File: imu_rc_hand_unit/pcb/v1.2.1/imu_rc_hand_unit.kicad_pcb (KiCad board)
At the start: 2 copper layers, 35 x 50 mm, 76 parts, among them J1 USB_C_Receptacle_USB2.0_16P, J2 JST SH1.0, Q1 IRLML6344TRPBF, Q2 IRLML6344TRPBF, Q3 DMP3160L-7, Q4 IRLML6344TRPBF, Q5 DMP3160L-7, Q6 BSS138, Q7 BC817-25, Q8 BC817-25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

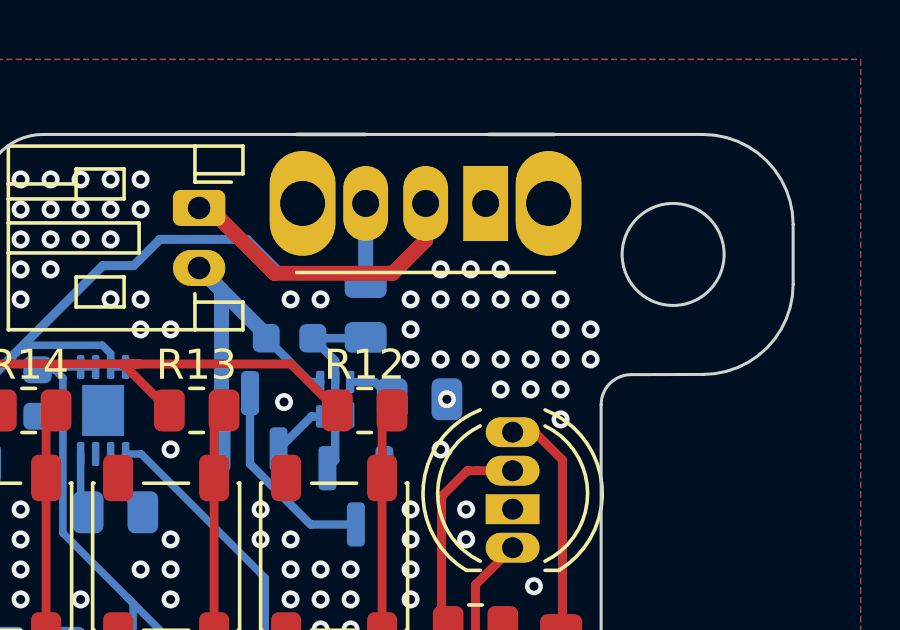
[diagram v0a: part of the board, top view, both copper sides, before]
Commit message: commit #39
imu rc hand unit v1.2.2:
removed bq297
added ON/OFF text for switch

enclosure hand unit:
small hole changes inside (m3) and outside (m3)
led diameter hole increased
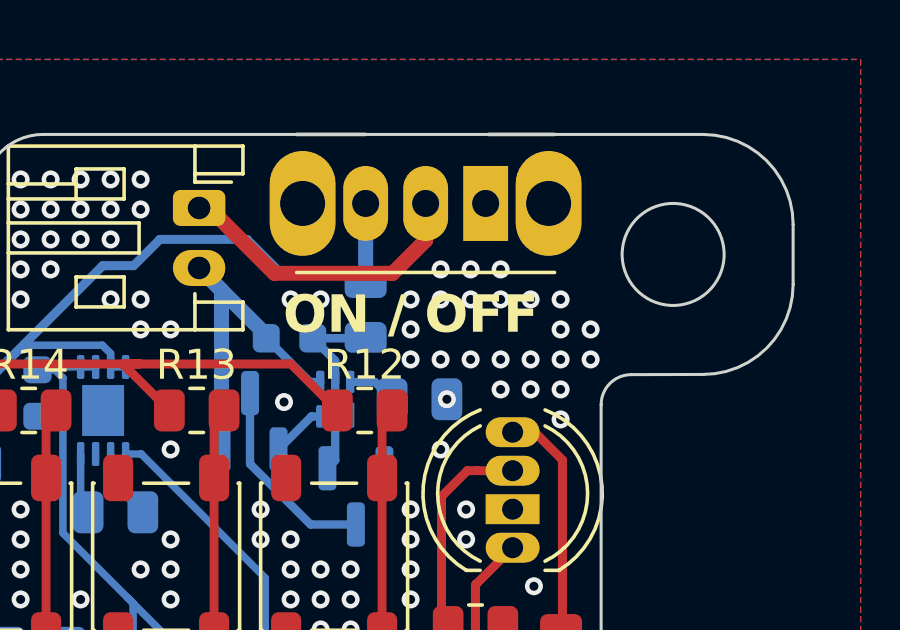
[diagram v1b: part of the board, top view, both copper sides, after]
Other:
- board text added: "ON / OFF"
- board text added: "v1.2.2"
- board text removed: "v1.2.1"
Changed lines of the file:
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@@
 		(layer "Margin")
+	)
+	(gr_text "ON / OFF"
+		(at 37.75 25.5 0)
+		(layer "F.SilkS")
+		(effects
+			(font
+				(size 1.25 1.25)
+				(thickness 0.25)
+				(bold yes)
+			)
+			(justify left)
+		)
 	)
 	(gr_text "IMU-RC \nHand Unit"
@@
 		)
 	)
-	(gr_text "v1.2.1"
+	(gr_text "v1.2.2"
 		(at 43.876582 43.816106 0)
 		(layer "B.SilkS")
